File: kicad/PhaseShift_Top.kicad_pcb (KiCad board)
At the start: 2 copper layers, 66.4 x 128.6 mm, 13 parts

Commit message: added MCU
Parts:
- moved SPMP1 200.0 mm to (375.5, 90.0)
- moved SPMP10 200.0 mm to (394.5, 171.0)
- moved SPMP11 200.0 mm to (375.5, 190.0)
- moved SPMP12 200.0 mm to (394.5, 190.0)
- moved SPMP13 200.0 mm to (413.6, 190.0)
- moved SPMP2 200.0 mm to (375.5, 113.8)
- moved SPMP3 200.0 mm to (375.5, 132.9)
- moved SPMP4 200.0 mm to (394.5, 90.0)
- moved SPMP5 200.0 mm to (394.5, 113.8)
- moved SPMP6 200.0 mm to (394.5, 132.9)
- moved SPMP7 200.0 mm to (413.6, 90.0)
- moved SPMP8 200.0 mm to (413.6, 113.8)
- moved SPMP9 200.0 mm to (413.6, 132.9)

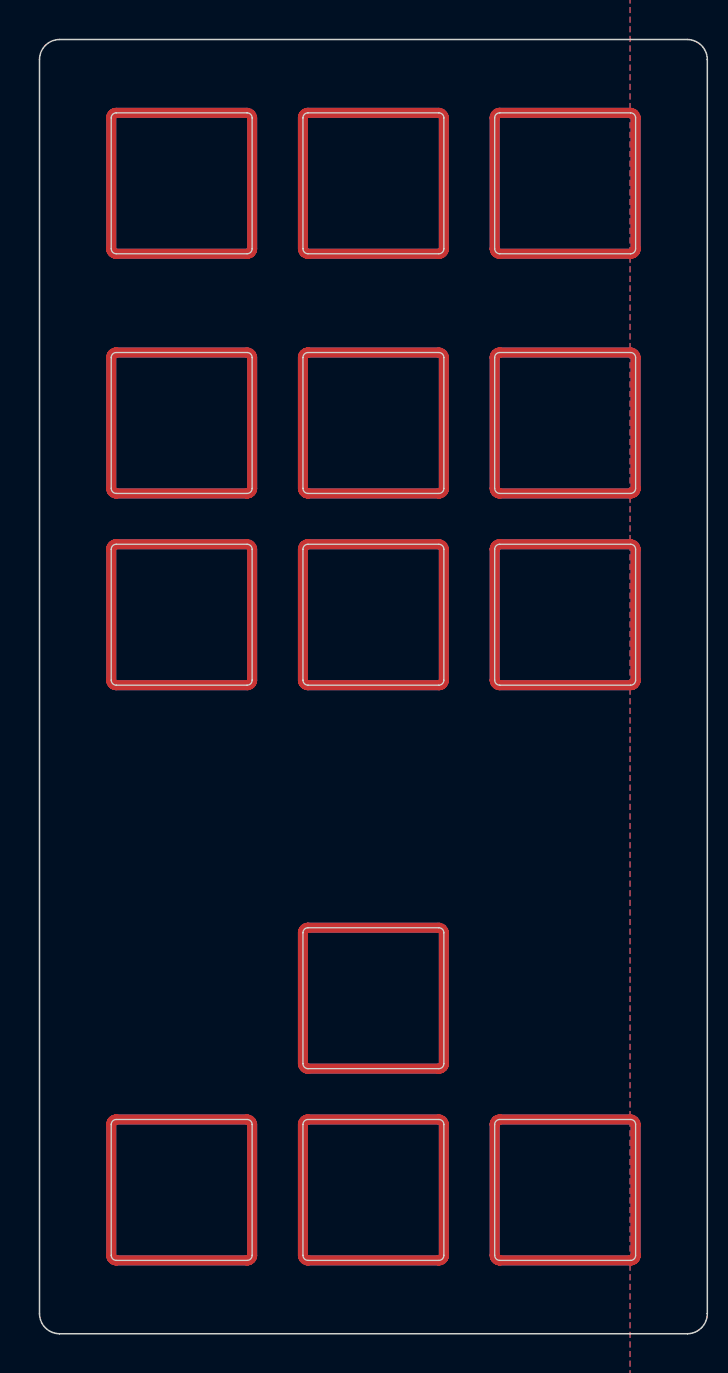
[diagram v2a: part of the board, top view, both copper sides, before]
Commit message: screw holes
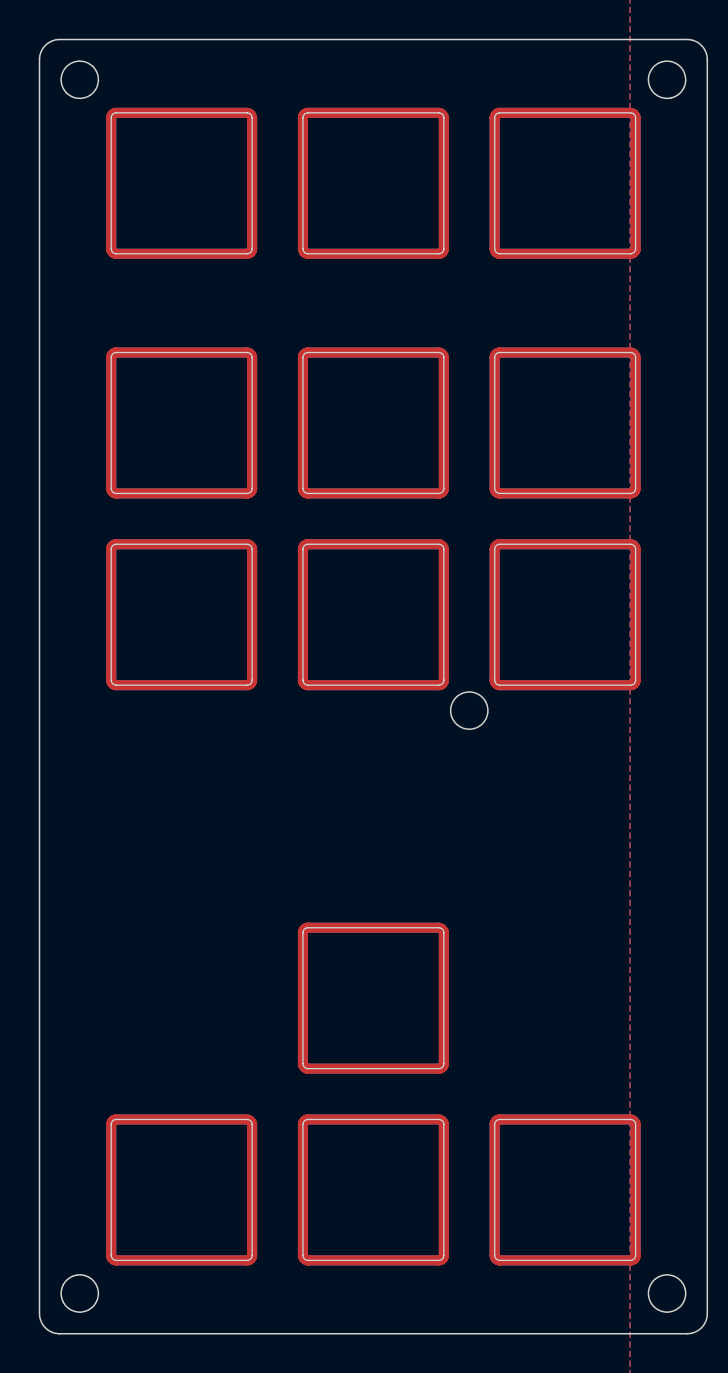
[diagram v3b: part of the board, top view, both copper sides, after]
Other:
- outline, holes or cut-outs redrawn
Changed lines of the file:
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@@
     (title "PhaseShift_Top")
     (date "2025-07-03")
-    (rev "0.3.4")
+    (rev "0.3.5")
     (company "Allen Choi")
   )
@@
 (gr_arc (start 425.67500000000007 204.29999999999998) (mid 427.08921360000005 203.7142136) (end 427.67500000000007 202.29999999999998) (layer Edge.Cuts) (stroke (width 0.15) (type default)))
 (gr_arc (start 361.32500000000005 202.29999999999998) (mid 361.91078640000006 203.7142136) (end 363.32500000000005 204.29999999999998) (layer Edge.Cuts) (stroke (width 0.15) (type default)))
+(gr_circle (center 365.32500000000005 79.7125) (end 367.17500000000007 79.7125) (layer Edge.Cuts) (stroke (width 0.15) (type default)) (fill none))
+(gr_circle (center 423.67500000000007 79.7125) (end 425.5250000000001 79.7125) (layer Edge.Cuts) (stroke (width 0.15) (type default)) (fill none))
+(gr_circle (center 423.67500000000007 200.29999999999998) (end 425.5250000000001 200.29999999999998) (layer Edge.Cuts) (stroke (width 0.15) (type default)) (fill none))
+(gr_circle (center 365.32500000000005 200.29999999999998) (end 367.17500000000007 200.29999999999998) (layer Edge.Cuts) (stroke (width 0.15) (type default)) (fill none))
+(gr_circle (center 404.02500000000003 142.38750000000002) (end 405.87500000000006 142.38750000000002) (layer Edge.Cuts) (stroke (width 0.15) (type default)) (fill none))
 )

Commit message: pogo pin - ergogen
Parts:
- moved SPMP1 190.0 mm to (185.4, 90.0)
- moved SPMP10 190.0 mm to (204.5, 171.0)
- moved SPMP11 190.0 mm to (185.4, 190.0)
- moved SPMP12 190.0 mm to (204.5, 190.0)
- moved SPMP13 190.0 mm to (223.6, 190.0)
- moved SPMP2 190.0 mm to (185.4, 113.8)
- moved SPMP3 190.0 mm to (185.4, 132.9)
- moved SPMP4 190.0 mm to (204.5, 90.0)
- moved SPMP5 190.0 mm to (204.5, 113.8)
- moved SPMP6 190.0 mm to (204.5, 132.9)
- moved SPMP7 190.0 mm to (223.6, 90.0)
- moved SPMP8 190.0 mm to (223.6, 113.8)
- moved SPMP9 190.0 mm to (223.6, 132.9)
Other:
- outline, holes or cut-outs redrawn

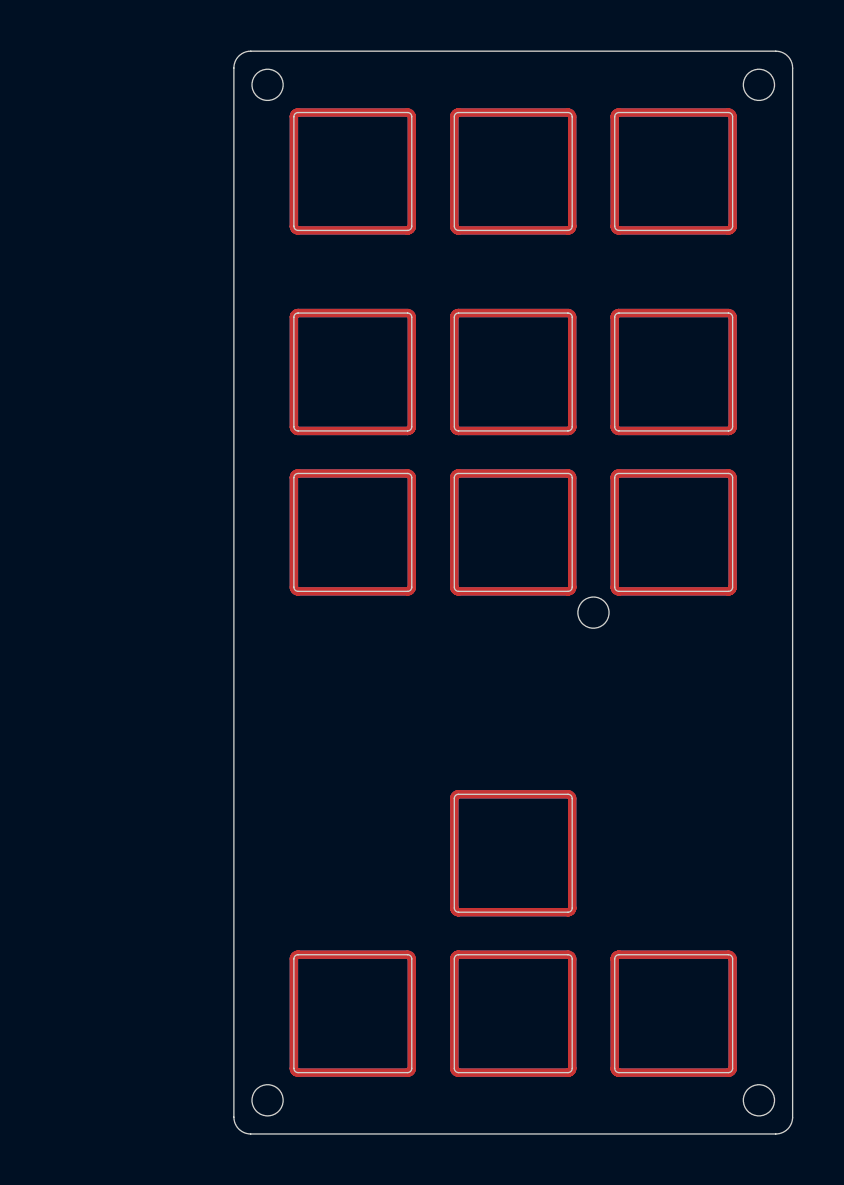
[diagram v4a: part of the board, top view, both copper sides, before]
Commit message: changed screw sizes
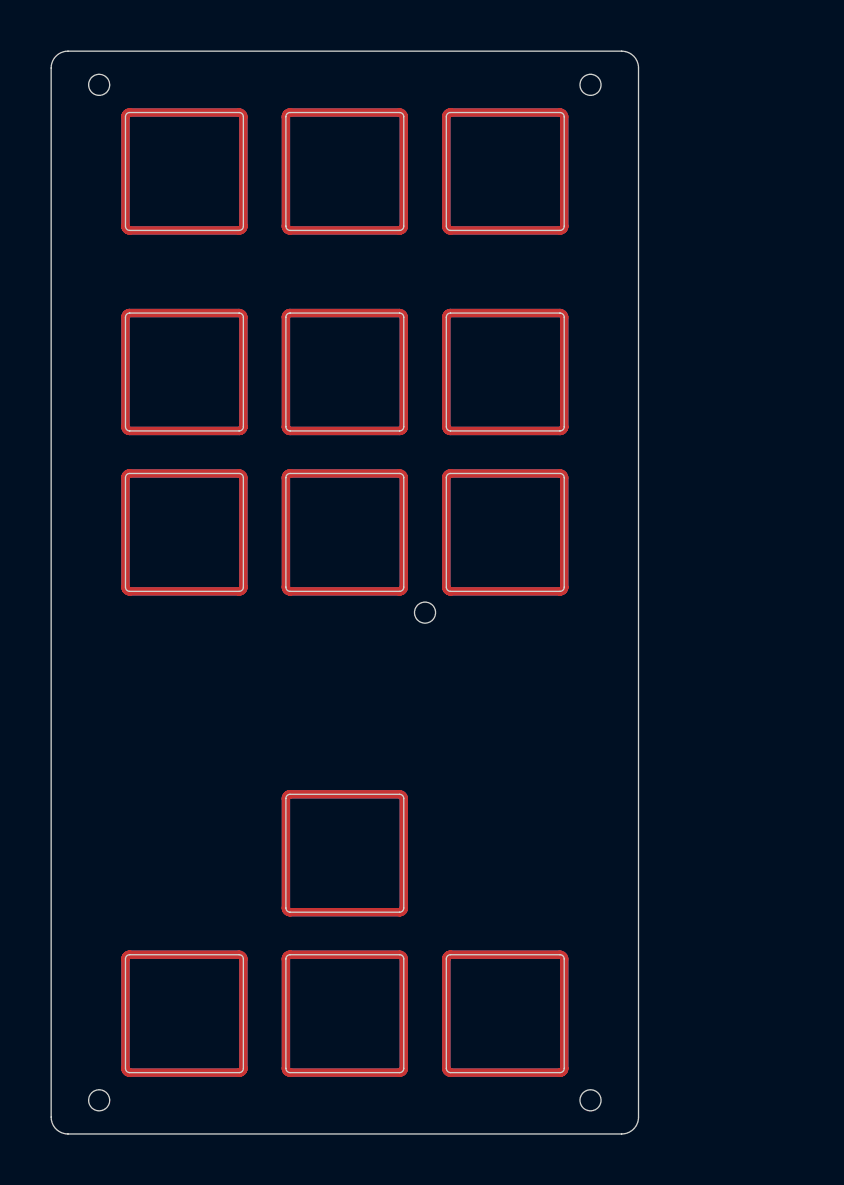
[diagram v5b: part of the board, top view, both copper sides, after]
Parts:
- moved SPMP1 20.0 mm to (165.4, 90.0)
- moved SPMP10 20.0 mm to (184.5, 171.0)
- moved SPMP11 20.0 mm to (165.4, 190.0)
- moved SPMP12 20.0 mm to (184.5, 190.0)
- moved SPMP13 20.0 mm to (203.6, 190.0)
- moved SPMP2 20.0 mm to (165.4, 113.8)
- moved SPMP3 20.0 mm to (165.4, 132.9)
- moved SPMP4 20.0 mm to (184.5, 90.0)
- moved SPMP5 20.0 mm to (184.5, 113.8)
- moved SPMP6 20.0 mm to (184.5, 132.9)
- moved SPMP7 20.0 mm to (203.6, 90.0)
- moved SPMP8 20.0 mm to (203.6, 113.8)
- moved SPMP9 20.0 mm to (203.6, 132.9)
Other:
- board size 66.4 x 128.6 mm -> 69.8 x 128.6 mm
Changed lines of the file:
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@@
 	(title_block
 		(title "PhaseShift_Top")
-		(date "2025-07-04")
-		(rev "0.3.6")
+		(date "2025-07-08")
+		(rev "0.4.3")
 		(company "Allen Choi")
 	)
@@
 	(footprint "Plate-MP_MX_1u"
 		(layer "F.Cu")
-		(at 223.55 190.0125)
-		(property "Reference" "SPMP13"
+		(at 184.5 170.9625)
+		(property "Reference" "SPMP10"
 			(at 0 -0.5 0)
 			(layer "F.SilkS")
@@
 	(footprint "Plate-MP_MX_1u"
 		(layer "F.Cu")
-		(at 223.55 113.8125)
-		(property "Reference" "SPMP8"
+		(at 203.55 190.0125)
+		(property "Reference" "SPMP13"
 			(at 0 -0.5 0)
 			(layer "F.SilkS")
@@
 	(footprint "Plate-MP_MX_1u"
 		(layer "F.Cu")
-		(at 185.45 190.0125)
-		(property "Reference" "SPMP11"
+		(at 203.55 90)
+		(property "Reference" "SPMP7"
 			(at 0 -0.5 0)
 			(layer "F.SilkS")
@@
 	(footprint "Plate-MP_MX_1u"
 		(layer "F.Cu")
-		(at 204.5 90)
-		(property "Reference" "SPMP4"
+		(at 165.45 190.0125)
+		(property "Reference" "SPMP11"
 			(at 0 -0.5 0)
 			(layer "F.SilkS")
@@
 	(footprint "Plate-MP_MX_1u"
 		(layer "F.Cu")
-		(at 204.5 132.8625)
-		(property "Reference" "SPMP6"
+		(at 165.45 113.8125)
+		(property "Reference" "SPMP2"
 			(at 0 -0.5 0)
 			(layer "F.SilkS")
@@
 	(footprint "Plate-MP_MX_1u"
 		(layer "F.Cu")
-		(at 185.45 132.8625)
-		(property "Reference" "SPMP3"
+		(at 184.5 90)
+		(property "Reference" "SPMP4"
 			(at 0 -0.5 0)
 			(layer "F.SilkS")
@@
 	(footprint "Plate-MP_MX_1u"
 		(layer "F.Cu")
-		(at 223.55 90)
-		(property "Reference" "SPMP7"
+		(at 184.5 132.8625)
+		(property "Reference" "SPMP6"
 			(at 0 -0.5 0)
 			(layer "F.SilkS")
@@
 	(footprint "Plate-MP_MX_1u"
 		(layer "F.Cu")
-		(at 185.45 113.8125)
-		(property "Reference" "SPMP2"
+		(at 165.45 132.8625)
+		(property "Reference" "SPMP3"
 			(at 0 -0.5 0)
 			(layer "F.SilkS")
@@
 	(footprint "Plate-MP_MX_1u"
 		(layer "F.Cu")
-		(at 223.55 132.8625)
-		(property "Reference" "SPMP9"
+		(at 184.5 190.0125)
+		(property "Reference" "SPMP12"
 			(at 0 -0.5 0)
 			(layer "F.SilkS")
@@
 	(footprint "Plate-MP_MX_1u"
 		(layer "F.Cu")
-		(at 204.5 113.8125)
+		(at 184.5 113.8125)
 		(property "Reference" "SPMP5"
 			(at 0 -0.5 0)
@@
 	(footprint "Plate-MP_MX_1u"
 		(layer "F.Cu")
-		(at 185.45 90)
-		(property "Reference" "SPMP1"
+		(at 203.55 132.8625)
+		(property "Reference" "SPMP9"
 			(at 0 -0.5 0)
 			(layer "F.SilkS")
@@
 	(footprint "Plate-MP_MX_1u"
 		(layer "F.Cu")
-		(at 204.5 190.0125)
-		(property "Reference" "SPMP12"
+		(at 203.55 113.8125)
+		(property "Reference" "SPMP8"
 			(at 0 -0.5 0)
 			(layer "F.SilkS")
@@
 	(footprint "Plate-MP_MX_1u"
 		(layer "F.Cu")
-		(at 204.5 170.9625)
-		(property "Reference" "SPMP10"
+		(at 165.45 90)
+		(property "Reference" "SPMP1"
 			(at 0 -0.5 0)
 			(layer "F.SilkS")
@@
 		(embedded_fonts no)
 	)
-	(gr_arc
-		(start 237.675 202.3)
-		(mid 237.089214 203.714214)
-		(end 235.675 204.3)
+	(gr_circle
+		(center 155.325 79.7125)
+		(end 156.575 79.7125)
 		(stroke
 			(width 0.15)
 			(type default)
 		)
+		(fill no)
 		(layer "Edge.Cuts")
 	)
-	(gr_circle
-		(center 175.325 200.3)
-		(end 177.175 200.3)
+	(gr_line
+		(start 149.625 202.3)
+		(end 149.625 77.7125)
 		(stroke
 			(width 0.15)
 			(type default)
 		)
-		(fill no)
 		(layer "Edge.Cuts")
 	)
 	(gr_circle
-		(center 233.675 200.3)
-		(end 235.525 200.3)
+		(center 155.325 200.3)
+		(end 156.575 200.3)
 		(stroke
 			(width 0.15)
@@
 	)
 	(gr_circle
-		(center 175.325 79.7125)
-		(end 177.175 79.7125)
+		(center 213.675 79.7125)
+		(end 214.925 79.7125)
 		(stroke
 			(width 0.15)
@@
 		(layer "Edge.Cuts")
 	)
-	(gr_line
-		(start 237.675 77.7125)
-		(end 237.675 202.3)
+	(gr_circle
+		(center 213.675 200.3)
+		(end 214.925 200.3)
 		(stroke
 			(width 0.15)
 			(type default)
 		)
+		(fill no)
 		(layer "Edge.Cuts")
 	)
-	(gr_line
-		(start 235.675 204.3)
-		(end 173.325 204.3)
+	(gr_circle
+		(center 194.025 142.3875)
+		(end 195.275 142.3875)
 		(stroke
 			(width 0.15)
 			(type default)
 		)
+		(fill no)
 		(layer "Edge.Cuts")
 	)
-	(gr_circle
-		(center 233.675 79.7125)
-		(end 235.525 79.7125)
+	(gr_arc
+		(start 151.625 204.3)
+		(mid 150.210786 203.714214)
+		(end 149.625 202.3)
 		(stroke
 			(width 0.15)
 			(type default)
 		)
-		(fill no)
 		(layer "Edge.Cuts")
 	)
 	(gr_line
-		(start 173.325 75.7125)
-		(end 235.675 75.7125)
+		(start 219.375 77.7125)
+		(end 219.375 202.3)
 		(stroke
 			(width 0.15)
@@
 		(layer "Edge.Cuts")
 	)
-	(gr_circle
-		(center 214.025 142.3875)
-		(end 215.875 142.3875)
+	(gr_line
+		(start 217.375 204.3)
+		(end 151.625 204.3)
 		(stroke
 			(width 0.15)
 			(type default)
 		)
-		(fill no)
 		(layer "Edge.Cuts")
 	)
 	(gr_arc
-		(start 171.325 77.7125)
-		(mid 171.910786 76.298286)
-		(end 173.325 75.7125)
+		(start 219.375 202.3)
+		(mid 218.789214 203.714214)
+		(end 217.375 204.3)
 		(stroke
 			(width 0.15)
@@
 		(layer "Edge.Cuts")
 	)
-	(gr_arc
-		(start 173.325 204.3)
-		(mid 171.910786 203.714214)
-		(end 171.325 202.3)
+	(gr_line
+		(start 151.625 75.7125)
+		(end 217.375 75.7125)
 		(stroke
 			(width 0.15)
@@
 	)
 	(gr_arc
-		(start 235.675 75.7125)
-		(mid 237.089214 76.298286)
-		(end 237.675 77.7125)
+		(start 149.625 77.7125)
+		(mid 150.210786 76.298286)
+		(end 151.625 75.7125)
 		(stroke
 			(width 0.15)
@@
 		(layer "Edge.Cuts")
 	)
-	(gr_line
-		(start 171.325 202.3)
-		(end 171.325 77.7125)
+	(gr_arc
+		(start 217.375 75.7125)
+		(mid 218.789214 76.298286)
+		(end 219.375 77.7125)
 		(stroke
 			(width 0.15)

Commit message: fixed positions for screw holes
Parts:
- moved SPMP1 210.0 mm to (375.5, 90.0)
- moved SPMP10 210.0 mm to (394.5, 171.0)
- moved SPMP11 210.0 mm to (375.5, 190.0)
- moved SPMP12 210.0 mm to (394.5, 190.0)
- moved SPMP13 210.0 mm to (413.6, 190.0)
- moved SPMP2 210.0 mm to (375.5, 113.8)
- moved SPMP3 210.0 mm to (375.5, 132.9)
- moved SPMP4 210.0 mm to (394.5, 90.0)
- moved SPMP5 210.0 mm to (394.5, 113.8)
- moved SPMP6 210.0 mm to (394.5, 132.9)
- moved SPMP7 210.0 mm to (413.6, 90.0)
- moved SPMP8 210.0 mm to (413.6, 113.8)
- moved SPMP9 210.0 mm to (413.6, 132.9)
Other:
- outline, holes or cut-outs redrawn

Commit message: more tweaks  (#3)
* small tweaks

* GlyphMatrix - 3mm screws

* PhaseShift - 3mm screws

* DeltaForm - 3mm screws

* updated README.md
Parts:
- moved SPMP1 210.0 mm to (165.4, 90.0)
- moved SPMP10 210.0 mm to (184.5, 171.0)
- moved SPMP11 210.0 mm to (165.4, 190.0)
- moved SPMP12 210.0 mm to (184.5, 190.0)
- moved SPMP13 210.0 mm to (203.6, 190.0)
- moved SPMP2 210.0 mm to (165.4, 113.8)
- moved SPMP3 210.0 mm to (165.4, 132.9)
- moved SPMP4 210.0 mm to (184.5, 90.0)
- moved SPMP5 210.0 mm to (184.5, 113.8)
- moved SPMP6 210.0 mm to (184.5, 132.9)
- moved SPMP7 210.0 mm to (203.6, 90.0)
- moved SPMP8 210.0 mm to (203.6, 113.8)
- moved SPMP9 210.0 mm to (203.6, 132.9)
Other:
- outline, holes or cut-outs redrawn

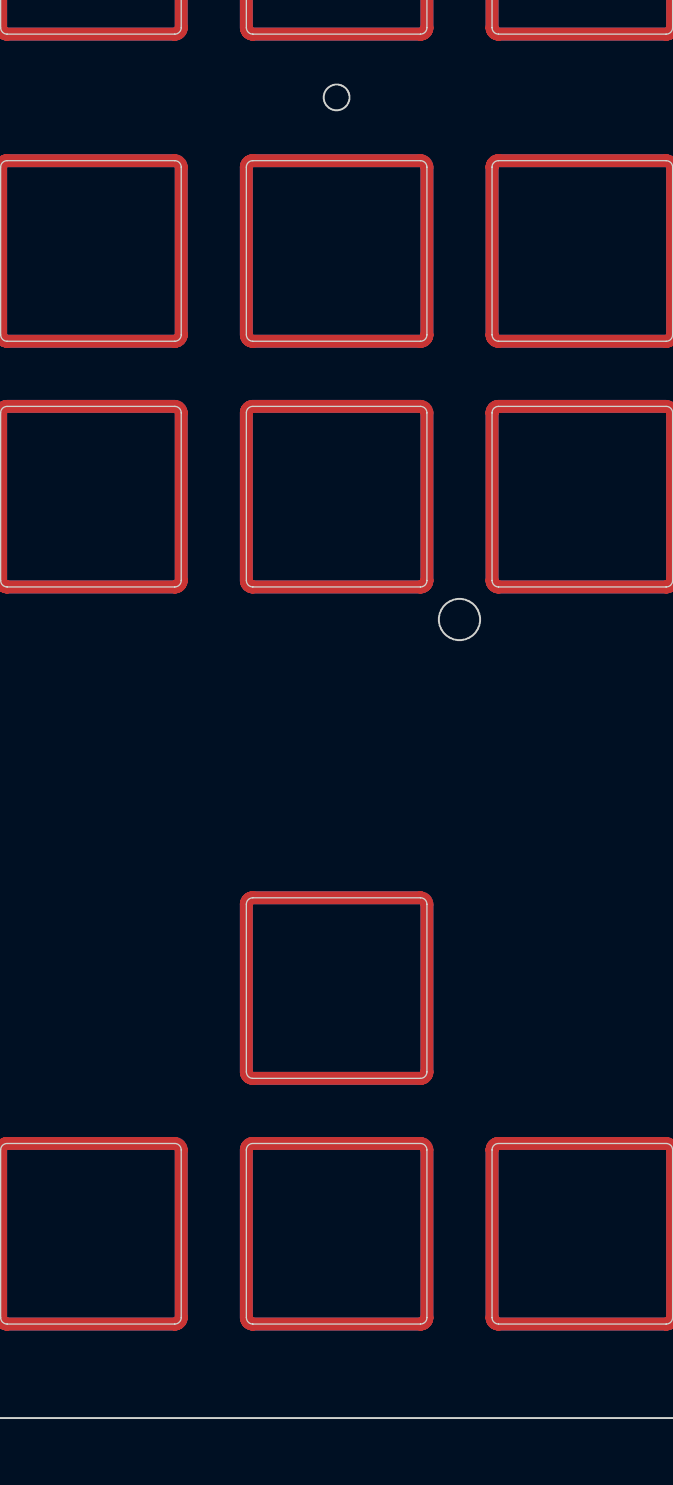
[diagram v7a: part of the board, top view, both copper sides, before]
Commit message: plates (#4)
* Silk Screen

* small changes for GlyphMatrix

* Silk screen for plates

* amended GlyphMatrix
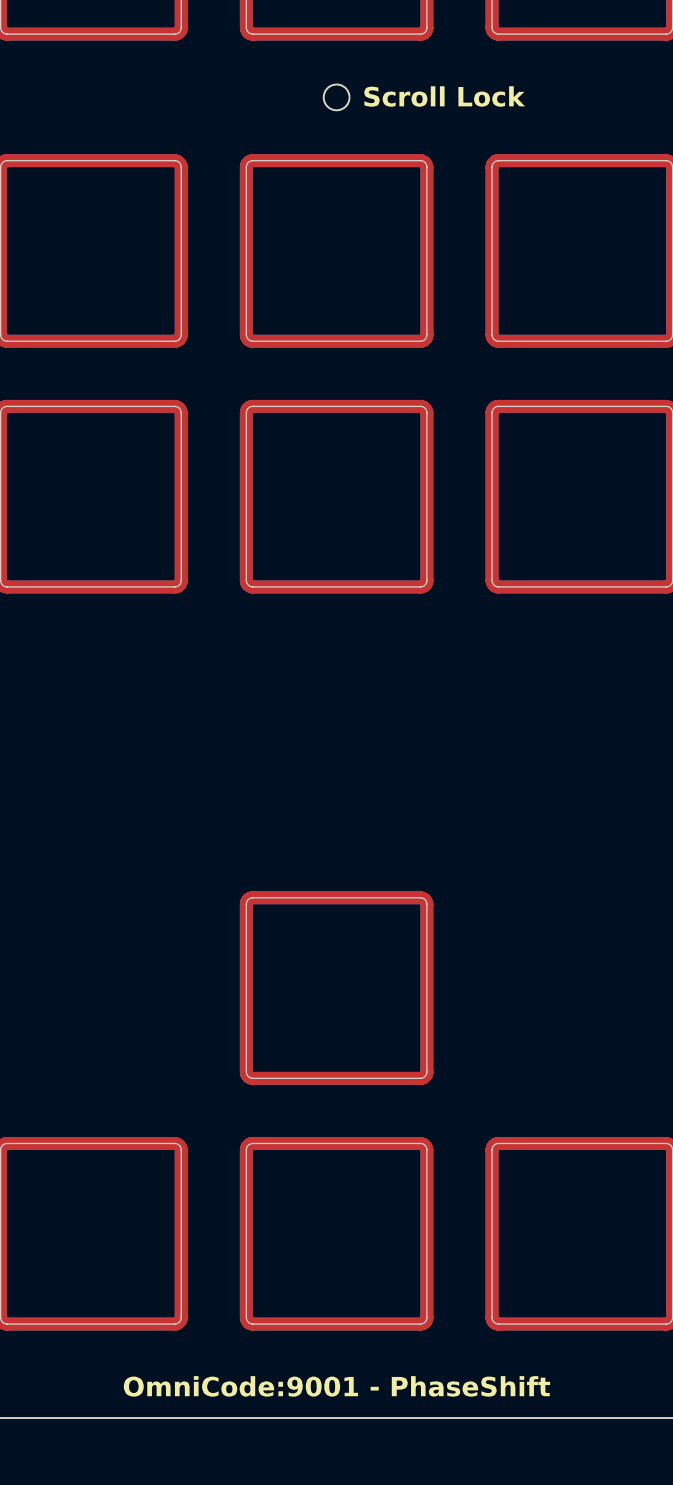
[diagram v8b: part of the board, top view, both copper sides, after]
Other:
- outline, holes or cut-outs redrawn
- board text added: "OmniCode:9001 - PhaseShift"
- board text added: "Scroll Lock"
